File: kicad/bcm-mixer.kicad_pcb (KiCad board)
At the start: 2 copper layers, 142 x 108.5 mm, 103 parts, among them J1 AudioJack2_SwitchT, J10 Conn_01x08_Pin, J11 Conn_01x08_Socket, J12 Conn_01x08_Socket, J13 Conn_01x08_Pin, J14 Conn_01x06_Pin, J15 Conn_01x06_Socket, J16 Conn_01x06_Socket, J17 Conn_01x06_Pin, J2 AudioJack2_SwitchT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

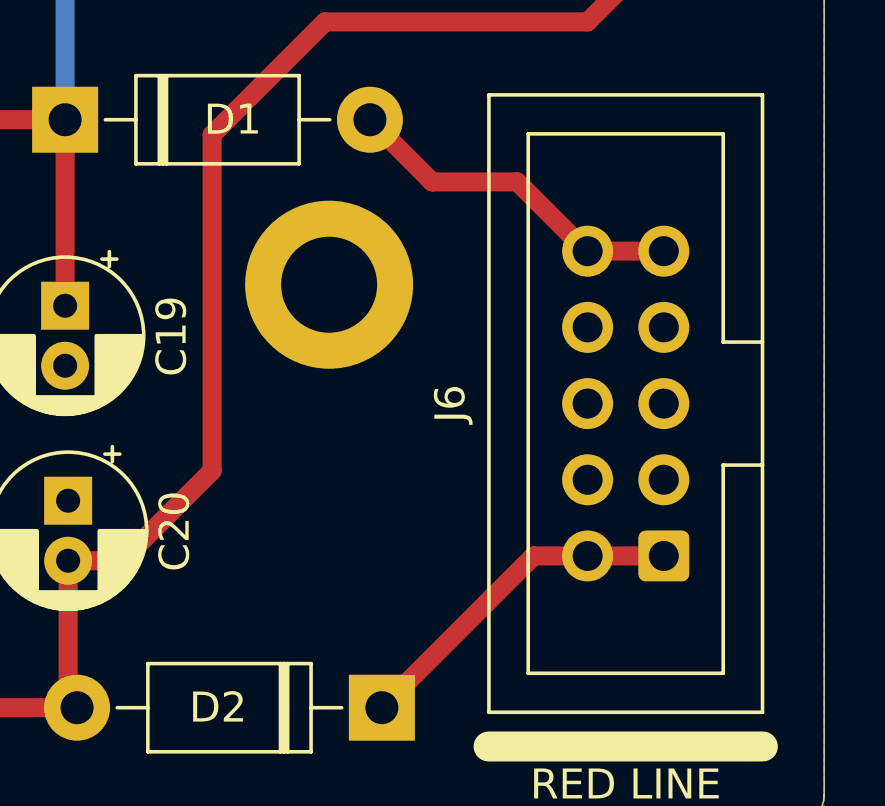
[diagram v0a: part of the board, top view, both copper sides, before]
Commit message: Updating power header symbol
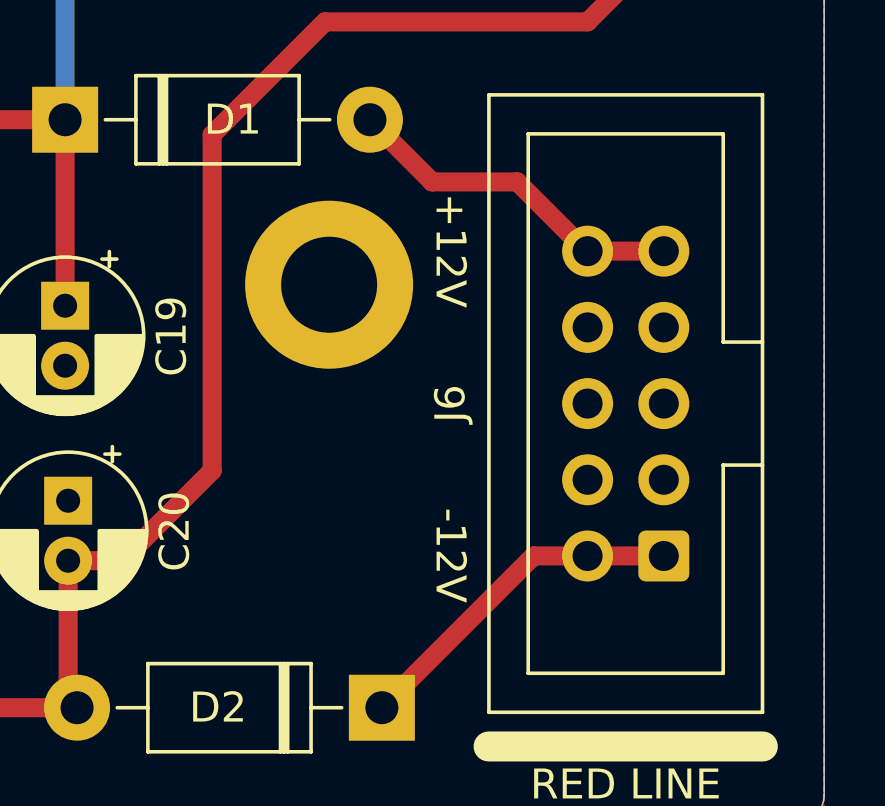
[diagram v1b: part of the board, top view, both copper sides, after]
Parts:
- J6: footprint Rumblesan_Eurorack_Power:Eurorack_PowerHeader_2x05_P2.54mm_Shrouded -> Rumblesan_Eurorack_Power:Eurorack_Power_IDC-Header_2x05_P2.54mm_Vertical
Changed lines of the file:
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@@
 		)
 	)
-	(footprint "Rumblesan_Eurorack_Power:Eurorack_PowerHeader_2x05_P2.54mm_Shrouded"
+	(footprint "Rumblesan_Eurorack_Power:Eurorack_Power_IDC-Header_2x05_P2.54mm_Vertical"
 		(layer "F.Cu")
 		(at 168.656 152.0415 180)
-		(descr "Through hole IDC box header, 2x05, 2.54mm pitch, DIN 41651 / IEC 60603-13, double rows, https://docs.google.com/spreadsheets/d/16SsEcesNF15N3Lb4niX7dcUr-NY5_MFPQhobNuNppn4/edit#gid=0")
-		(tags "Through hole vertical IDC box header THT 2x05 2.54mm double row")
+		(descr "Through hole IDC box header, 2x05, 2.54mm pitch, DIN 41651 / IEC 60603-13, double rows with silkscreen for eurorack power")
+		(tags "Through hole vertical IDC box header THT 2x05 2.54mm double row eurorack")
 		(property "Reference" "J6"
 			(at 7.112 5.08 90)
@@
 			(at 1.27 16.26 180)
 			(layer "F.Fab")
-			(hide yes)
 			(effects
 				(font
@@
 			)
 		)
-		(property "Footprint" "Rumblesan_Eurorack_Power:Eurorack_PowerHeader_2x05_P2.54mm_Shrouded"
+		(property "Footprint" "Rumblesan_Eurorack_Power:Eurorack_Power_IDC-Header_2x05_P2.54mm_Vertical"
 			(at 0 0 180)
 			(layer "F.Fab")
@@
 			(layer "F.Fab")
 		)
+		(fp_text user "+12V"
+			(at 7.112 10.1825 -90)
+			(unlocked yes)
+			(layer "F.SilkS")
+			(effects
+				(font
+					(size 1 1)
+					(thickness 0.15)
+				)
+			)
+		)
+		(fp_text user "-12V"
+			(at 7.112 0.0225 -90)
+			(unlocked yes)
+			(layer "F.SilkS")
+			(effects
+				(font
+					(size 1 1)
+					(thickness 0.15)
+				)
+			)
+		)
 		(fp_text user "RED LINE"
 			(at 1.27 -7.62 0)
@@
 			(net 0)
 			(net_name "")
-			(layers "B.Cu" "B.Adhes" "B.Paste" "B.SilkS" "B.Mask")
+			(layers "B.Cu" "B.SilkS" "B.Mask")
 			(hatch edge 0.508)
 			(connect_pads
@@
 			(net 0)
 			(net_name "")
-			(layers "B.Cu" "B.Adhes" "B.Paste" "B.SilkS" "B.Mask")
+			(layers "B.Cu" "B.SilkS" "B.Mask")
 			(hatch edge 0.508)
 			(connect_pads
@@
 			(net 0)
 			(net_name "")
-			(layers "B.Cu" "B.Adhes" "B.Paste" "B.SilkS" "B.Mask")
+			(layers "B.Cu" "B.SilkS" "B.Mask")
 			(hatch edge 0.508)
 			(connect_pads
@@
 			(net 0)
 			(net_name "")
-			(layers "B.Cu" "B.Adhes" "B.Paste" "B.SilkS" "B.Mask")
+			(layers "B.Cu" "B.SilkS" "B.Mask")
 			(hatch edge 0.508)
 			(connect_pads
@@
 			(net 0)
 			(net_name "")
-			(layers "B.Cu" "B.Adhes" "B.Paste" "B.SilkS" "B.Mask")
+			(layers "B.Cu" "B.SilkS" "B.Mask")
 			(hatch edge 0.508)
 			(connect_pads
@@
 			(net 0)
 			(net_name "")
-			(layers "B.Cu" "B.Adhes" "B.Paste" "B.SilkS" "B.Mask")
+			(layers "B.Cu" "B.SilkS" "B.Mask")
 			(hatch edge 0.508)
 			(connect_pads

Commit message: Updating for revision 2
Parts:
- added H5: MountingHole, MountingHole:MountingHole_3.2mm_M3_DIN965, F.Cu at (50.5, 143.0)
- C1, C21: value 1uF -> 10uF
- C10, C2, C3, C4: value 10pF -> 22pF
- R10, R11, R16, R17: value 3k3 -> 22k
- R12, R13, R24, R25: value 12k -> 22k
- R14, R15, R29, R30, R4, R5, R8, R9: value 10k -> 100k
- R18, R22: value 47k -> 100k
- R19, R23: value 220k -> 100k
- R27, R6: value 2k2 -> 10k
- RV1: value 10kA -> 50kA
- RV3, RV6: value 100kA -> 50kA
- RV4: value 10k -> 50kA
- moved C1 2.00 mm to (164.6, 63.5), turned to -90 degrees
- moved C21 2.00 mm to (146.8, 63.5), turned to -90 degrees
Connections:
- C1 pad 1: Net-(C1-Pad1) -> /CHAN1_INPUT_MAIN
- C1 pad 2: /CHAN1_INPUT_MAIN -> Net-(C1-Pad2)
- C21 pad 1: Net-(C21-Pad1) -> /CHAN2_INPUT_MAIN
- C21 pad 2: /CHAN2_INPUT_MAIN -> Net-(C21-Pad2)
- R27 pad 1: Net-(C21-Pad1) -> Net-(C21-Pad2)
- R6 pad 1: Net-(C1-Pad1) -> Net-(C1-Pad2)
- RV1 pad 1: GND -> /MAIN_R_LEVEL_CW_CTRL
- RV1 pad 3: /MAIN_R_LEVEL_CW_CTRL -> GND
- RV1 pad 4: GND -> /MAIN_L_LEVEL_CW_CTRL
- RV1 pad 6: /MAIN_L_LEVEL_CW_CTRL -> GND
- RV3 pad 1: GND -> /CHAN1_LEVEL_CW_CTRL
- RV3 pad 3: /CHAN1_LEVEL_CW_CTRL -> GND
- RV4 pad 1: GND -> /CHAN3_R_OUTPUT_CTRL
- RV4 pad 3: /CHAN3_R_OUTPUT_CTRL -> GND
- RV6 pad 1: GND -> /CHAN2_LEVEL_CW_CTRL
- RV6 pad 3: /CHAN2_LEVEL_CW_CTRL -> GND
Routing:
- net /CHAN1_LEVEL_CW_CTRL: track 79.4 -> 20.8 mm
- net /CHAN2_LEVEL_CW_CTRL: track 78.2 -> 20.8 mm
- net /MAIN_R_LEVEL_CW_CTRL: track 13.0 -> 69.3 mm
- net /MAIN_L_LEVEL_CW_CTRL: track 14.1 -> 69.5 mm
- net /CHAN3_R_OUTPUT_CTRL: track 70.8 -> 25.9 mm
- net Net-(C21-Pad2): track 0.00 -> 3.81 mm
- net Net-(C21-Pad1): track 3.81 -> 0.00 mm
- net Net-(C1-Pad2): track 0.00 -> 3.81 mm
- net Net-(C1-Pad1): track 3.81 -> 0.00 mm
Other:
- board text added: "${COMPANY} ${TITLE} ${REVISION}"
- board text removed: "BCM Mixer Rev01"
- board text removed: "Bristol Communal Modular"
